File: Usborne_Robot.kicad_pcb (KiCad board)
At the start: 2 copper layers, 128.3 x 81.3 mm, 36 parts, among them J1 C64, J2 BBC, J3 Motor Battery, J4 Relay Battery, J5 To Robot, K1 ARM, K2 GRIPPER, K3 LEFT, K4 RIGHT, K5 DIRECTION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

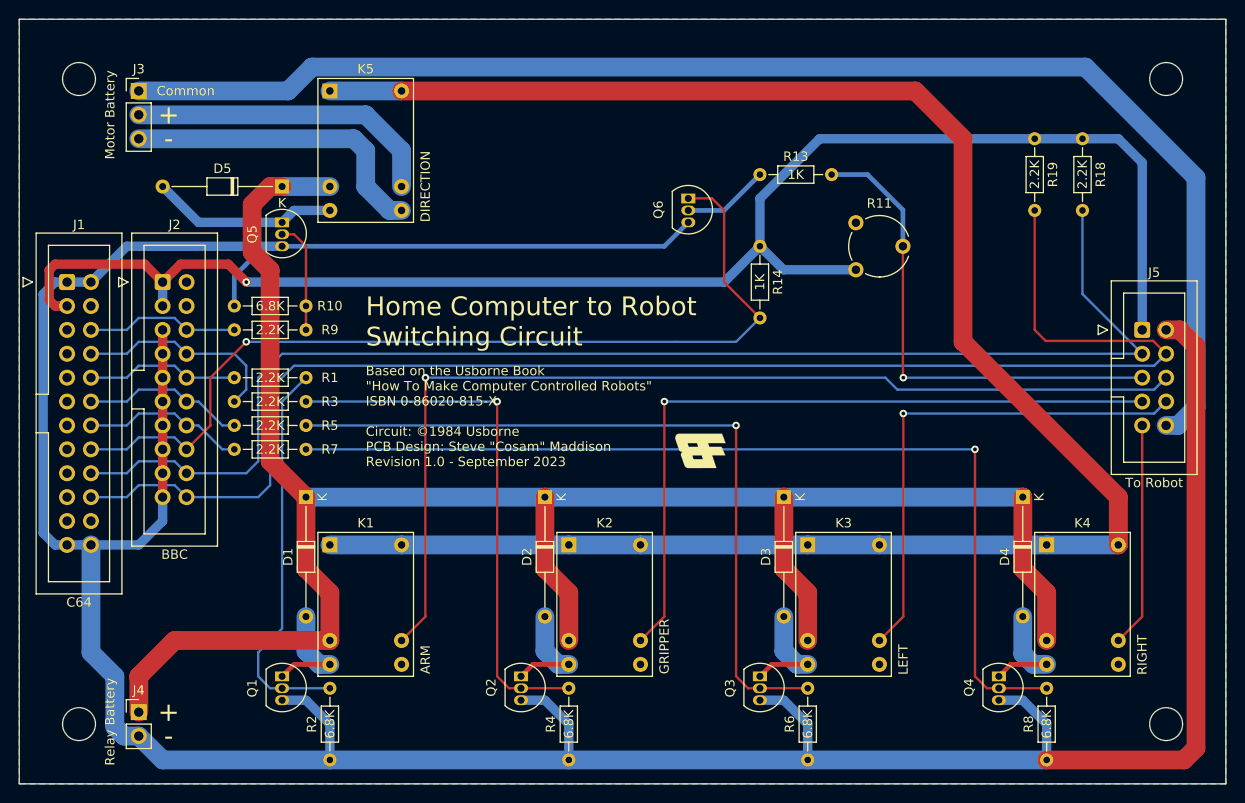
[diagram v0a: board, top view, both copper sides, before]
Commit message: Thicker traces for motor signals, wide footprints for transistors.
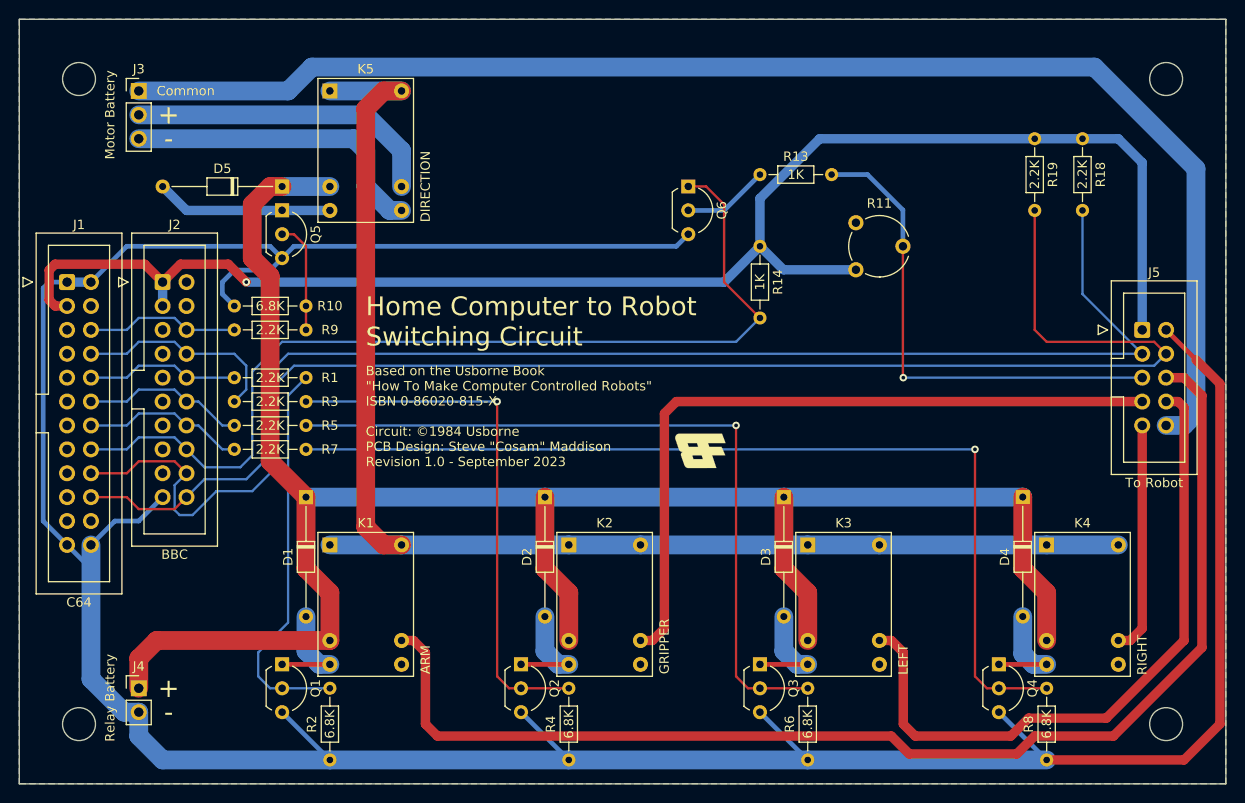
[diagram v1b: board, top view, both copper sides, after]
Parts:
- Q1, Q2, Q3, Q4, Q5, Q6: footprint Package_TO_SOT_THT:TO-92L_Inline -> Package_TO_SOT_THT:TO-92L_Inline_Wide
- moved J4 2.54 mm to (114.3, 127.0)
- moved Q5 1.28 mm to (129.5, 76.2)
- moved Q6 1.28 mm to (172.7, 73.7)
- moved Q1 1.27 mm to (129.5, 124.5)
- moved Q2 1.27 mm to (154.9, 124.5)
- moved Q3 1.27 mm to (180.3, 124.5)
- moved Q4 1.27 mm to (205.7, 124.5)
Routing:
- net MOTOR: track 203.3 -> 145.1 mm
- net GND: track 365.0 -> 340.6 mm
- net MOTOR_ARM: track 108.8 -> 130.6 mm, vias 1 -> 0
- net MOTOR_LEFT: track 53.6 -> 72.2 mm, vias 1 -> 0
- net PB6: track 155.3 -> 161.3 mm
- net PB5: track 98.3 -> 103.0 mm, vias 1 -> 0
- net +12V: track 209.6 -> 208.2 mm
- net PB7: track 141.2 -> 142.2 mm
- net Net-(D5-A): track 19.9 -> 18.8 mm
- net MOTOR_COMMON: track 146.7 -> 147.7 mm
- net MOTOR_RIGHT: track 23.9 -> 24.7 mm
- net Net-(D4-A): track 12.6 -> 12.0 mm
- net Net-(D3-A): track 12.4 -> 11.9 mm
- net Net-(D2-A): track 12.4 -> 11.9 mm
- net Net-(D1-A): track 12.4 -> 11.9 mm
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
